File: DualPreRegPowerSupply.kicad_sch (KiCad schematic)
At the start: 6 parts, among them J101 Banana_Red, J102 Banana_Black

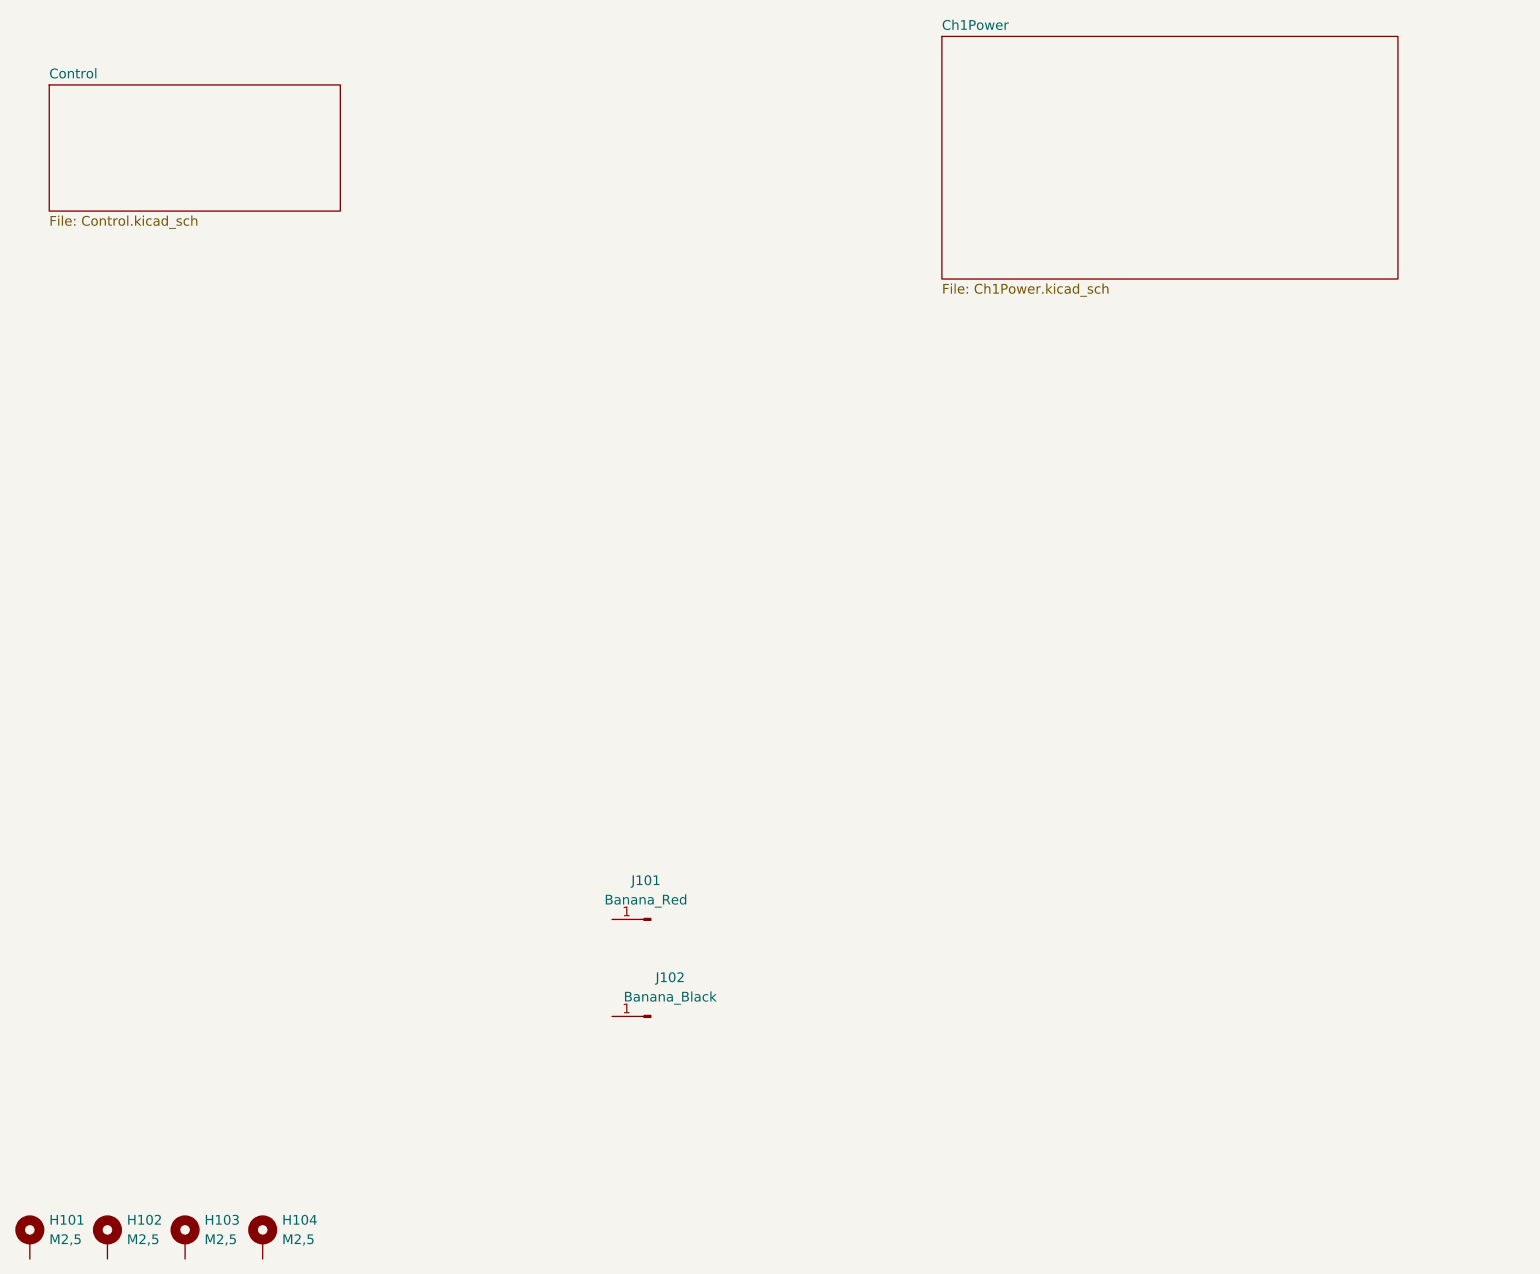
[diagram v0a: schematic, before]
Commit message: changed pass element drive
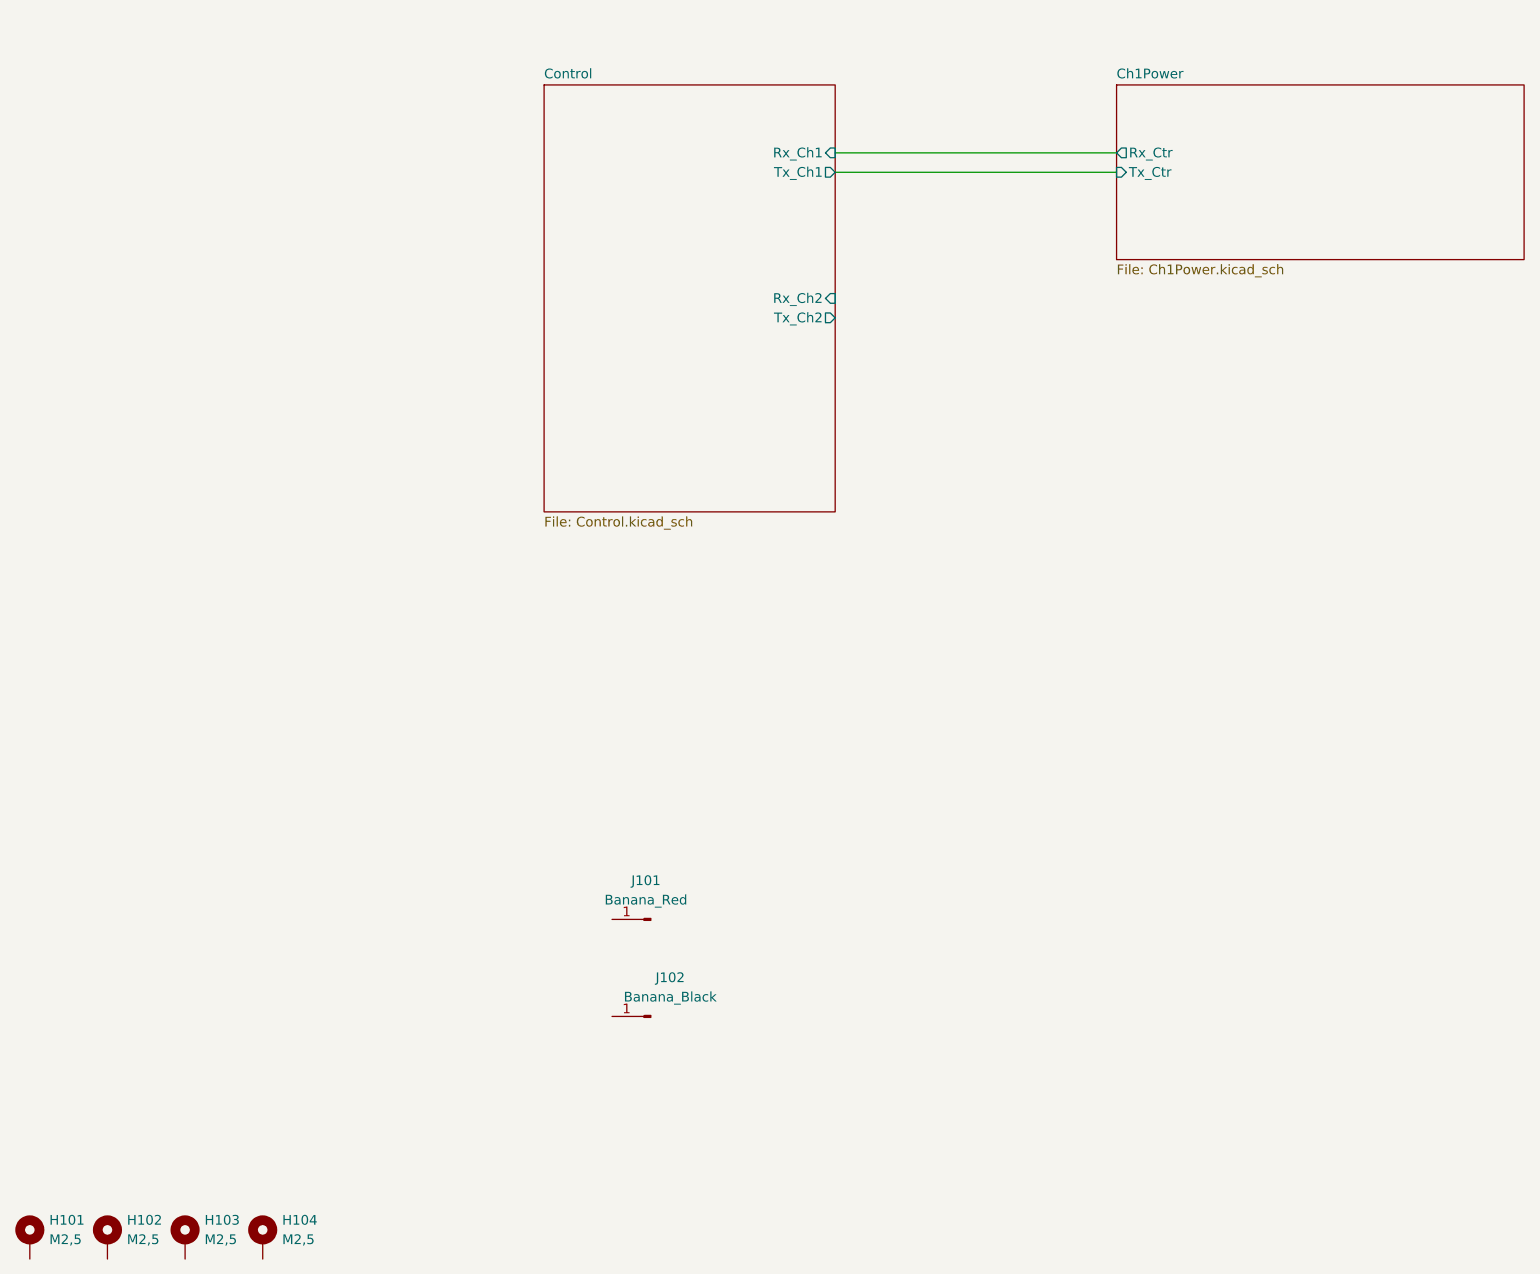
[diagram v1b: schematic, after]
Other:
- sheet Ch1Power ports: added Rx_Ctr, Tx_Ctr; removed none
- sheet Control ports: added Rx_Ch1, Rx_Ch2, Tx_Ch1, Tx_Ch2; removed none
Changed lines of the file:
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@@
 	(generator_version "10.0")
 	(paper "A4")
+	(wire
+		(pts
+			(xy 138.43 49.53) (xy 175.26 49.53)
+		)
+		(stroke
+			(width 0)
+			(type default)
+		)
+	)
+	(wire
+		(pts
+			(xy 138.43 46.99) (xy 175.26 46.99)
+		)
+		(stroke
+			(width 0)
+			(type default)
+		)
+	)
 	(symbol
 		(lib_id "Mechanical:MountingHole_Pad")
@@
 	)
 	(sheet
-		(at 152.4 31.75)
-		(size 59.69 31.75)
+		(at 175.26 38.1)
+		(size 53.34 22.86)
 		(exclude_from_sim no)
 		(in_bom yes)
@@
 		)
 		(property "Sheetname" "Ch1Power"
-			(at 152.4 31.0384 0)
+			(at 175.26 37.3884 0)
 			(show_name no)
 			(do_not_autoplace no)
@@
 		)
 		(property "Sheetfile" "Ch1Power.kicad_sch"
-			(at 152.4 64.0846 0)
+			(at 175.26 61.5446 0)
 			(show_name no)
 			(do_not_autoplace no)
@@
 				)
 				(justify left top)
+			)
+		)
+		(pin "Rx_Ctr" output
+			(at 175.26 46.99 180)
+			(effects
+				(font
+					(size 1.27 1.27)
+				)
+				(justify left)
+			)
+		)
+		(pin "Tx_Ctr" input
+			(at 175.26 49.53 180)
+			(effects
+				(font
+					(size 1.27 1.27)
+				)
+				(justify left)
 			)
 		)
@@
 	)
 	(sheet
-		(at 35.56 38.1)
-		(size 38.1 16.51)
+		(at 100.33 38.1)
+		(size 38.1 55.88)
 		(exclude_from_sim no)
 		(in_bom yes)
@@
 		)
 		(property "Sheetname" "Control"
-			(at 35.56 37.3884 0)
+			(at 100.33 37.3884 0)
 			(show_name no)
 			(do_not_autoplace no)
@@
 		)
 		(property "Sheetfile" "Control.kicad_sch"
-			(at 35.56 55.1946 0)
+			(at 100.33 94.5646 0)
 			(show_name no)
 			(do_not_autoplace no)
@@
 		)
 		(property "Field2" ""
-			(at 35.56 38.1 0)
-			(show_name no)
-			(do_not_autoplace no)
-			(effects
-				(font
-					(size 1.27 1.27)
-				)
-			)
-		)
+			(at 100.33 38.1 0)
+			(show_name no)
+			(do_not_autoplace no)
+			(effects
+				(font
+					(size 1.27 1.27)
+				)
+			)
+		)
+		(pin "Rx_Ch1" input
+			(at 138.43 46.99 0)
+			(effects
+				(font
+					(size 1.27 1.27)
+				)
+				(justify right)
+			)
+		)
+		(pin "Rx_Ch2" input
+			(at 138.43 66.04 0)
+			(effects
+				(font
+					(size 1.27 1.27)
+				)
+				(justify right)
+			)
+		)
+		(pin "Tx_Ch1" output
+			(at 138.43 49.53 0)
+			(effects
+				(font
+					(size 1.27 1.27)
+				)
+				(justify right)
+			)
+		)
+		(pin "Tx_Ch2" output
+			(at 138.43 68.58 0)
+			(effects
+				(font
+					(size 1.27 1.27)
+				)
+				(justify right)
+			)
+		)

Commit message: added Ch2 and removed global power flags
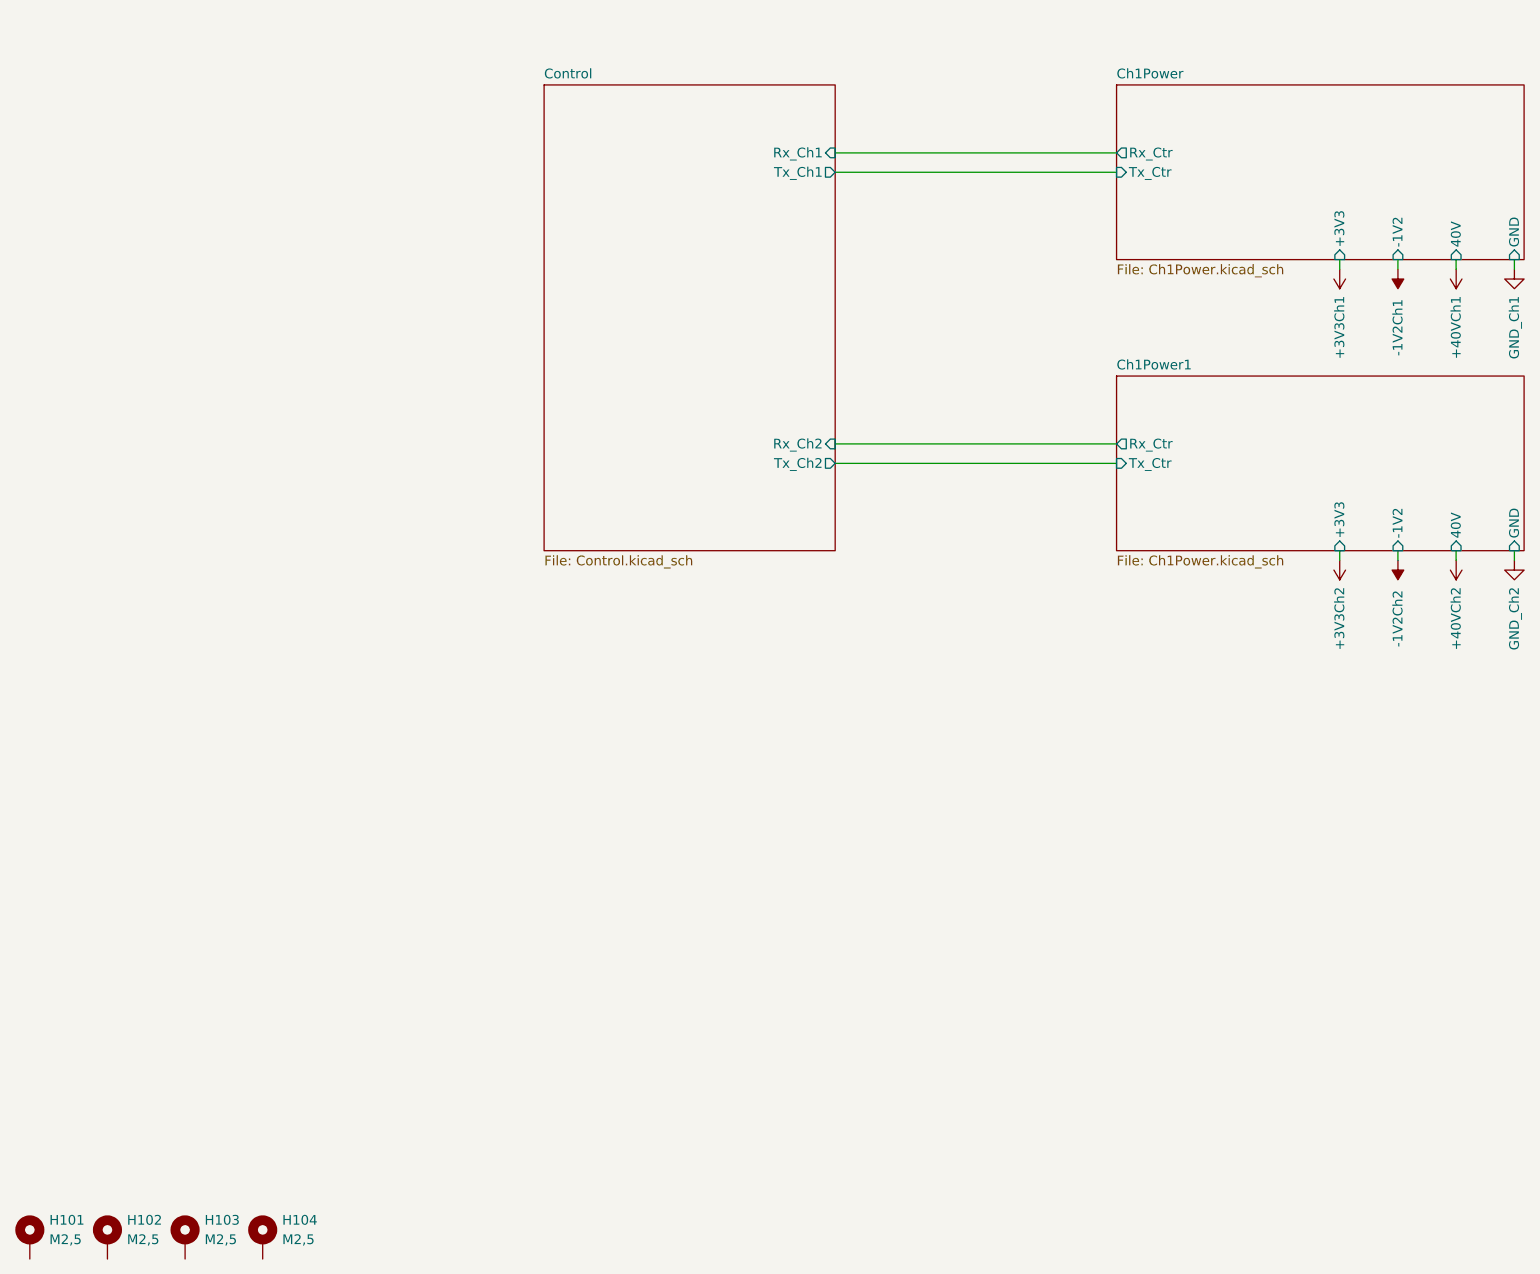
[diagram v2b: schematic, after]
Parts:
- removed J101: Banana_Red, Connector:Banana_Cliff_FCR7350R_S16N-PC_Horizontal, symbol Connector:Conn_01x01_Pin
- removed J102: Banana_Black, Connector:Banana_Cliff_FCR7350B_S16N-PC_Horizontal, symbol Connector:Conn_01x01_Pin
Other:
- added sheet Ch1Power1 (Ch1Power.kicad_sch)
- sheet Ch1Power ports: added +3V3, -1V2, 40V, GND; removed none
